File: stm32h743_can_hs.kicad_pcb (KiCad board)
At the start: 4 copper layers, 99.1 x 53.3 mm, 102 parts, among them J1 Conn_02x38_Counter_Clockwise, J2 Conn_02x38_Counter_Clockwise, J3 USB_C_Receptacle_USB2.0_16P, J4 USB_C_Receptacle_USB2.0_16P, J5 DE9_Pins_MH, J6 Conn_01x05_Pin, J7 Conn_ARM_JTAG_SWD_10, Q1 BSS138, Q2 BSS138, Q3 BSS138, SW1 SW_Push, SW2 SW_Push, U1 STM32H743IITx, U2 ST1S40IDR, U3 TPS2121RUX, U4 USB3300-EZK, U5 MCP2562-E-SN, U6 S25FL128LAGMFI013, Y1 SG-210STF, Y2 8MHz, Y3 Crystal

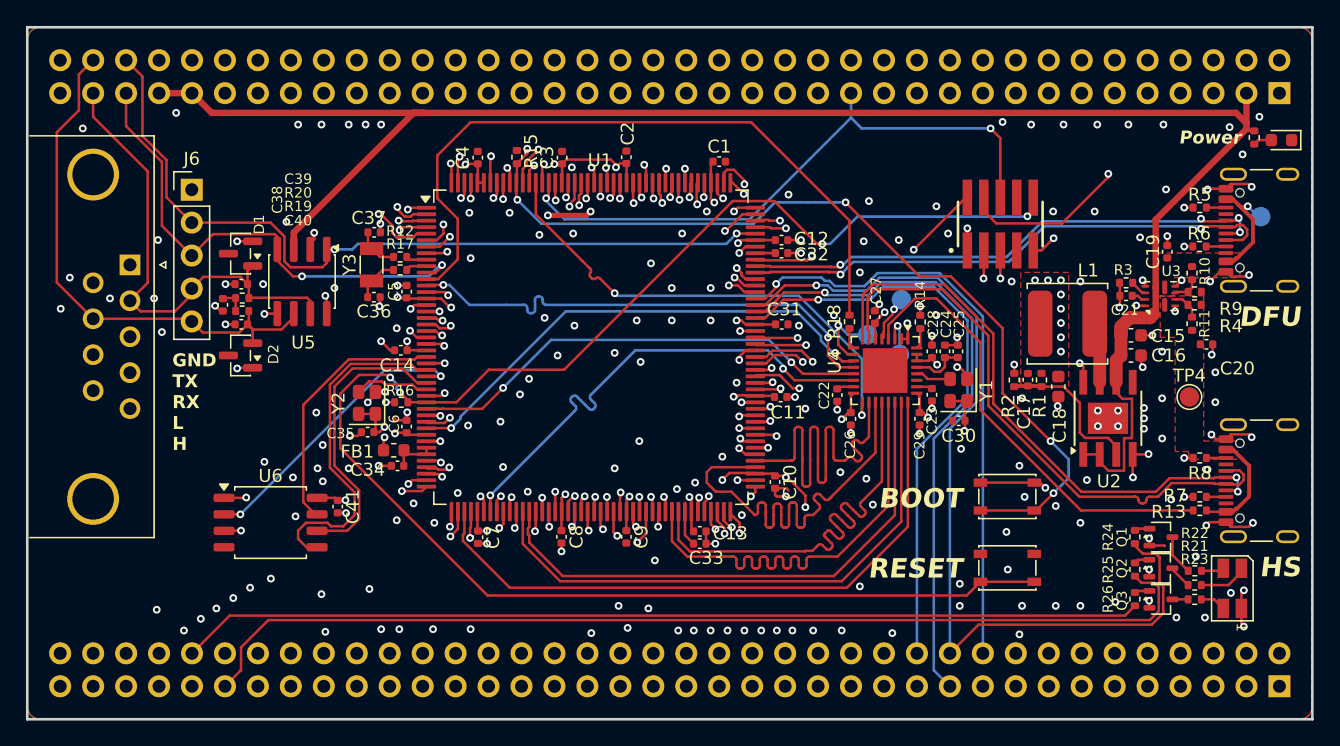
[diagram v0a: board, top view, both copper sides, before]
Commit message: board cleanup, change can xciever to TI
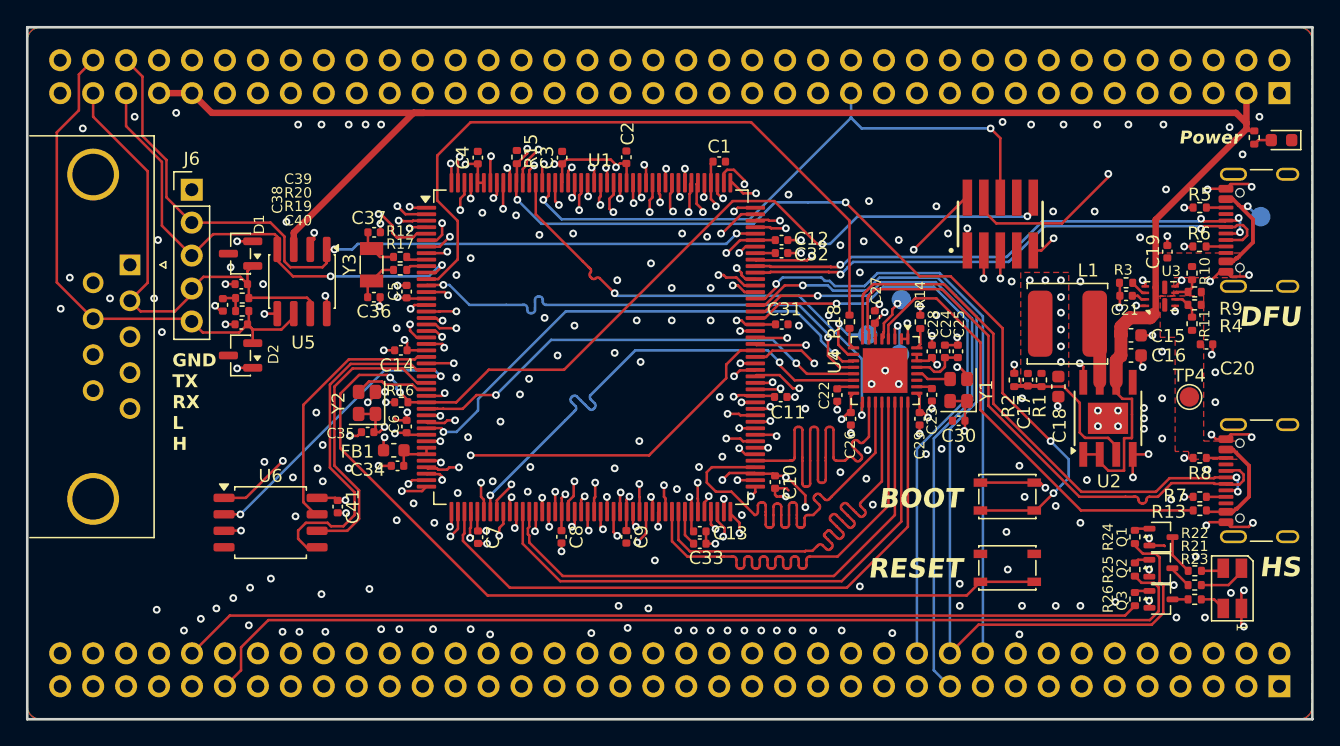
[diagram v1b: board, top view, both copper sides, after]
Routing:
- net +3V3: track 90.6 -> 86.7 mm, vias 43 -> 40
- net /PG3: track 29.2 -> 32.4 mm
- net /PA9: track 51.6 -> 54.2 mm
- net /PF1: track 21.2 -> 23.8 mm
- net /PD7: track 34.8 -> 37.3 mm
- net /PA6: track 107.0 -> 109.5 mm
- net /PD0: track 42.5 -> 44.8 mm
- net /PC10: track 40.0 -> 42.3 mm
- net /PH6: track 23.4 -> 25.8 mm
- net /PF13: track 33.8 -> 36.0 mm
- net /PG1: track 29.5 -> 31.7 mm
- net /PD8: track 23.0 -> 25.2 mm
- net /PD3: track 37.1 -> 39.2 mm
- net /PA4: track 35.1 -> 37.2 mm
- net /PE11: track 23.2 -> 25.2 mm
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
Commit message: cleanup
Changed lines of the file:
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@@
 	)
 	(via
-		(at 130.7 87.5)
+		(at 131.6 86.3)
 		(size 0.6)
 		(drill 0.3)
@@
 	)
 	(segment
-		(start 125.717188 111.382812)
-		(end 125.6 111.5)
+		(start 125.2 110.5)
+		(end 125.555314 110.5)
 		(width 0.2)
 		(layer "F.Cu")
@@
 	)
 	(segment
-		(start 125.717188 110.338126)
-		(end 125.717188 111.382812)
+		(start 125.555314 110.5)
+		(end 125.717188 110.338126)
 		(width 0.2)
 		(layer "F.Cu")
@@
 	)
 	(via
-		(at 125.6 111.5)
+		(at 125.2 110.5)
 		(size 0.6)
 		(drill 0.3)
@@
 	)
 	(segment
-		(start 125.6 111.5)
-		(end 124.95 112.15)
+		(start 110.35 112.15)
+		(end 101.9 120.6)
+		(width 0.2)
+		(layer "In2.Cu")
+		(net "/PH4")
+	)
+	(segment
+		(start 125.2 110.5)
+		(end 125.2 111.9)
 		(width 0.2)
 		(layer "In2.Cu")
@@
 	)
 	(segment
-		(start 110.35 112.15)
-		(end 101.9 120.6)
+		(start 124.95 112.15)
+		(end 110.35 112.15)
 		(width 0.2)
 		(layer "In2.Cu")
@@
 	)
 	(segment
-		(start 101.9 120.6)
-		(end 101.9 122.52)
+		(start 125.2 111.9)
+		(end 124.95 112.15)
 		(width 0.2)
 		(layer "In2.Cu")
@@
 	)
 	(segment
-		(start 124.95 112.15)
-		(end 110.35 112.15)
+		(start 101.9 120.6)
+		(end 101.9 122.52)
 		(width 0.2)
 		(layer "In2.Cu")
@@
 	)
 	(segment
-		(start 131.503572 83.644956)
-		(end 131.217188 83.93134)
+		(start 131.503572 83.340792)
+		(end 131.503572 83.644956)
 		(width 0.2)
 		(layer "F.Cu")
@@
 	)
 	(segment
-		(start 131.503572 83.340792)
-		(end 131.503572 83.644956)
+		(start 132.727209 82.4)
+		(end 132.444364 82.4)
+		(width 0.2)
+		(layer "F.Cu")
+		(net "/PB7")
+	)
+	(segment
+		(start 132.444364 82.4)
+		(end 131.503572 83.340792)
 		(width 0.2)
 		(layer "F.Cu")
@@
 	)
 	(segment
-		(start 132.422182 82.422182)
-		(end 131.503572 83.340792)
+		(start 131.503572 83.644956)
+		(end 131.217188 83.93134)
 		(width 0.2)
 		(layer "F.Cu")
@@
 	)
 	(via
-		(at 132.422182 82.422182)
+		(at 132.727209 82.4)
 		(size 0.6)
 		(drill 0.3)
@@
 	)
 	(segment
-		(start 132.6 82.6)
-		(end 132.810052 82.6)
-		(width 0.2)
-		(layer "In1.Cu")
-		(net "/PB7")
-	)
-	(segment
 		(start 152.75 79.35)
 		(end 152.75 76.77)
@@
 	)
 	(segment
-		(start 132.422182 82.422182)
-		(end 132.6 82.6)
+		(start 133.010052 82.4)
+		(end 133.110052 82.3)
 		(width 0.2)
 		(layer "In1.Cu")
@@
 	)
 	(segment
-		(start 132.810052 82.6)
-		(end 133.110052 82.3)
+		(start 132.727209 82.4)
+		(end 133.010052 82.4)
 		(width 0.2)
 		(layer "In1.Cu")
@@
 	)
 	(segment
-		(start 152.75 76.77)
-		(end 153.98 75.54)
+		(start 149.8 82.3)
+		(end 152.75 79.35)
 		(width 0.2)
 		(layer "In1.Cu")
@@
 	)
 	(segment
-		(start 149.8 82.3)
-		(end 152.75 79.35)
+		(start 152.75 76.77)
+		(end 153.98 75.54)
 		(width 0.2)
 		(layer "In1.Cu")

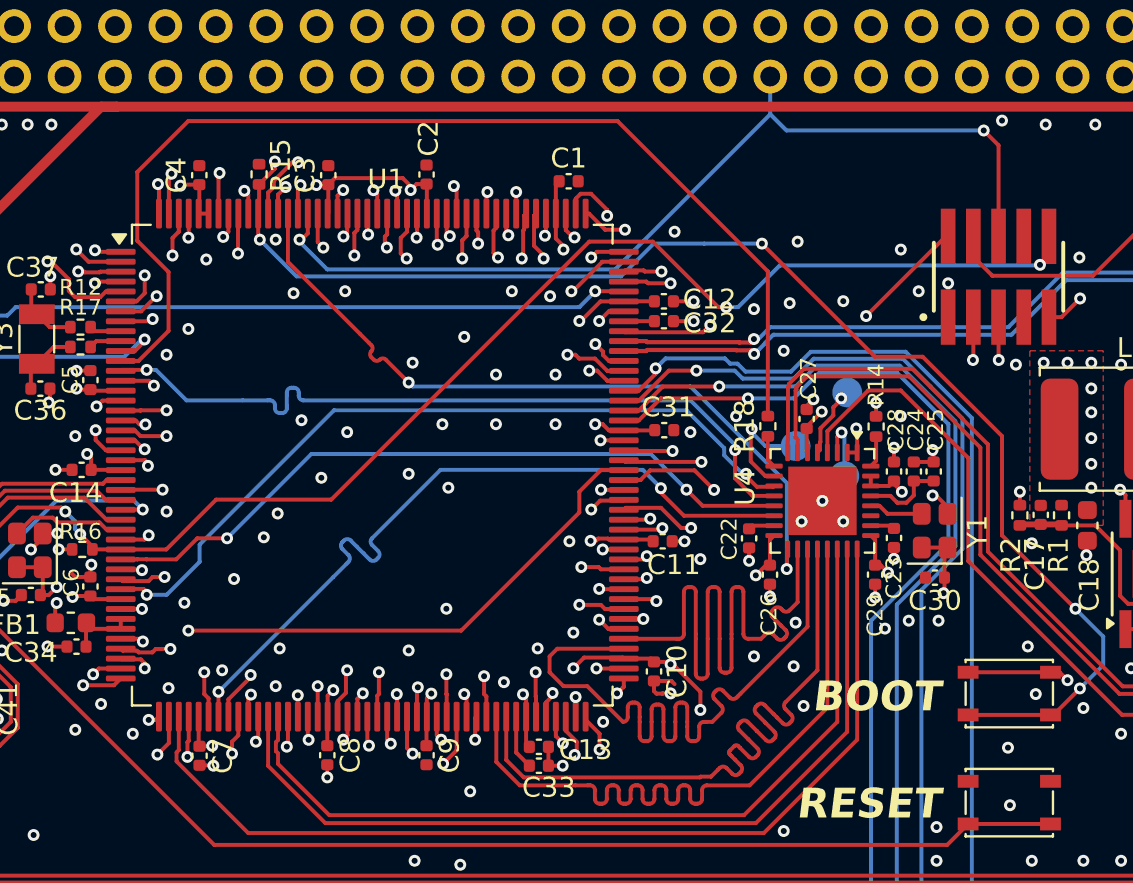
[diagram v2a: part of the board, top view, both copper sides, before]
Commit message: update pinion outputs, pcb cleanup
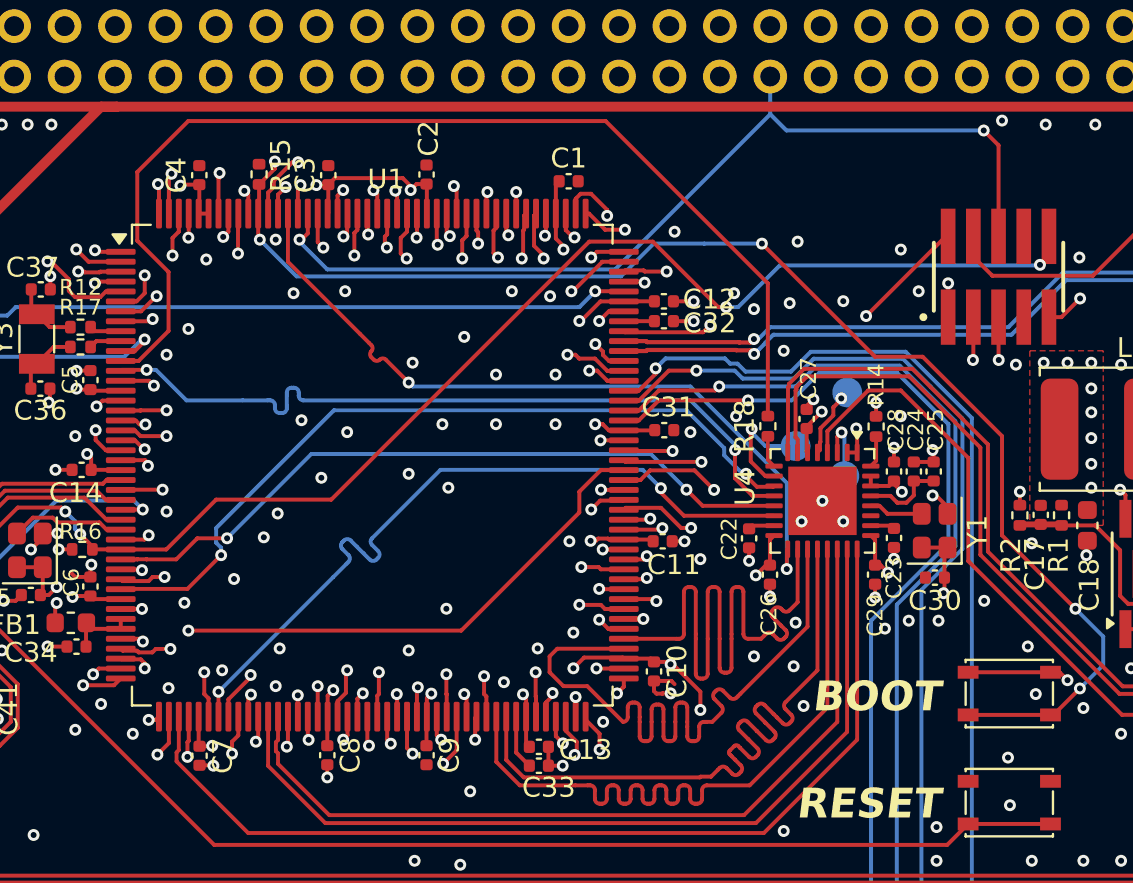
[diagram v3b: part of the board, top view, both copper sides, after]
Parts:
- U5: value MCP2562-E-SN -> TCAN1044AVDRQ1
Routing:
- net /PF3: track 25.1 -> 24.3 mm
- net GND: vias 250 -> 252
